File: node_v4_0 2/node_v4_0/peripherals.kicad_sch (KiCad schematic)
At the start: 26 parts, among them J3 Conn_Coaxial, U10 MCP7940N-xP, U11 1042240820, U12 CAT24M01W, U6 RFM69HCW, U9 SIM7080G

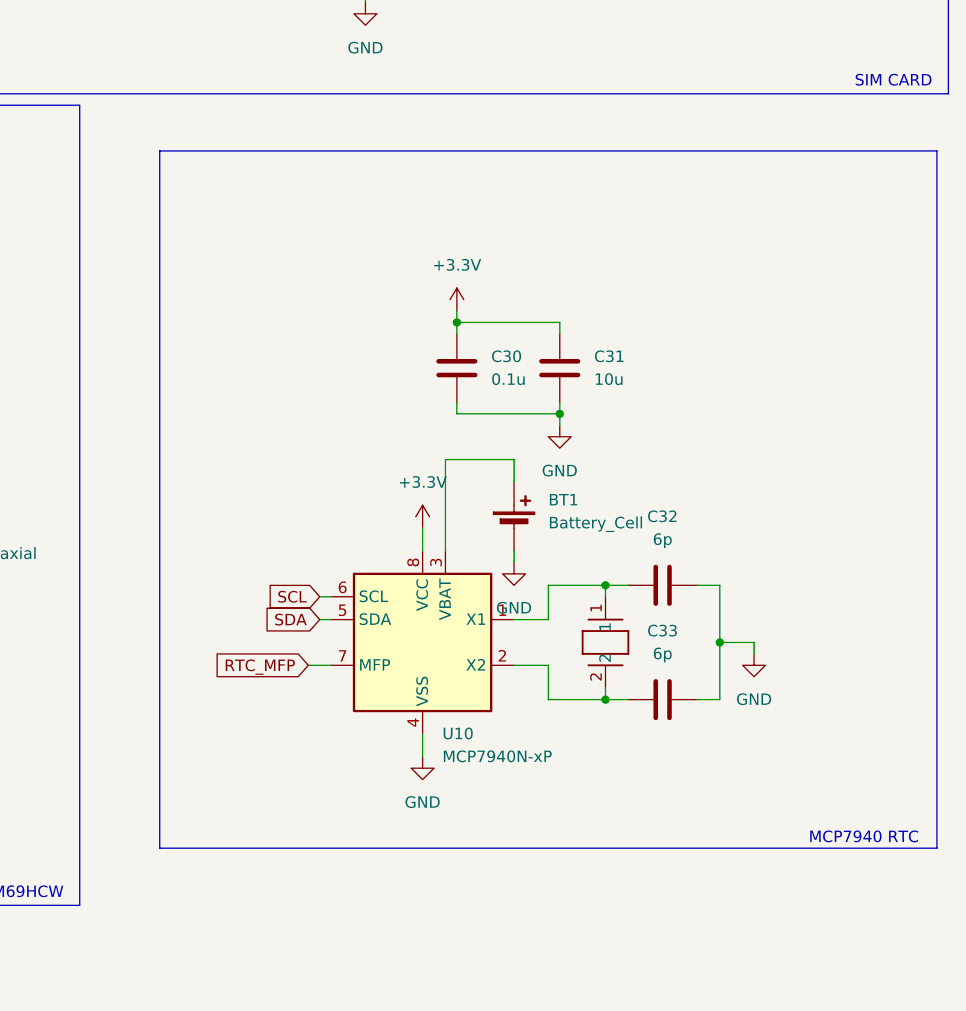
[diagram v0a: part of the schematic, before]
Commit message: finished laying out the board
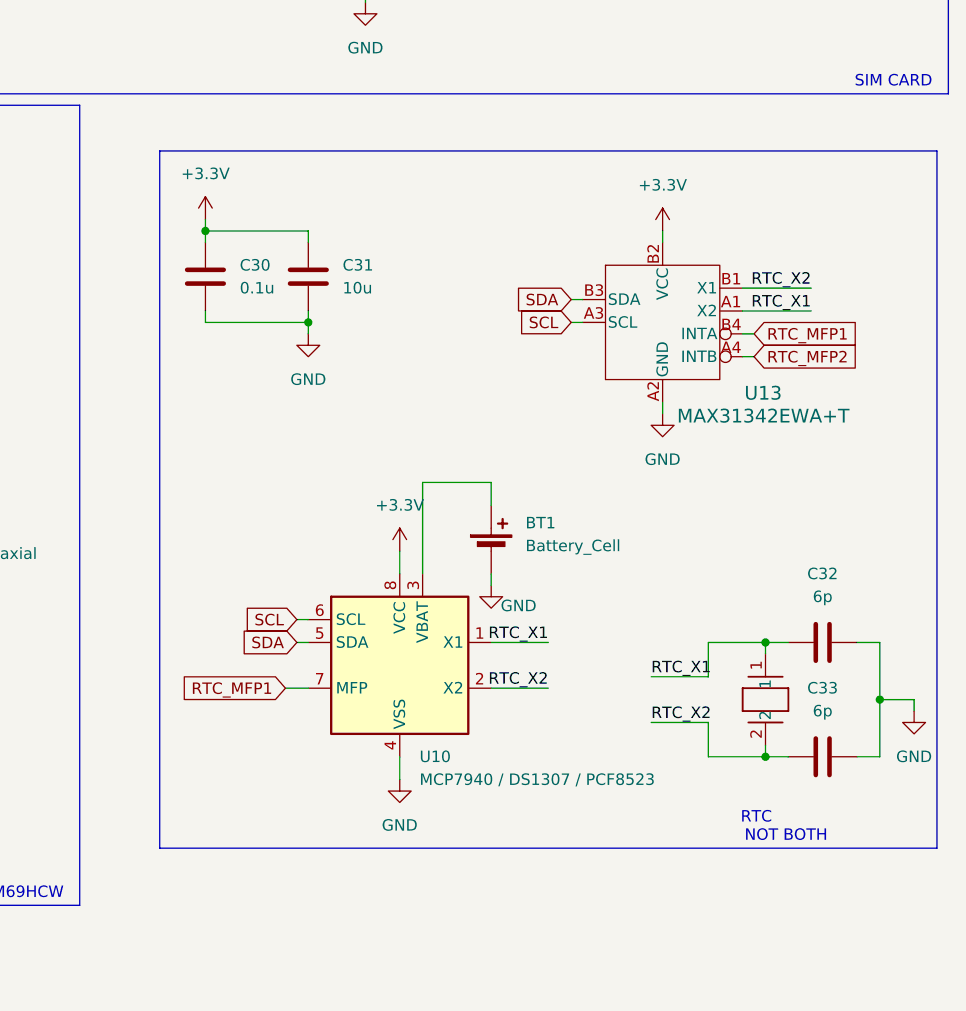
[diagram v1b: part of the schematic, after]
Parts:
- added U13: MAX31342EWA+T, WiSDOM:21-100291_W80D&plus_1_MXM, symbol WiSDOM:MAX31342EWA+T
- R14, R15: footprint Resistor_SMD:R_0805_2012Metric_Pad1.20x1.40mm_HandSolder -> Resistor_SMD:R_0402_1005Metric_Pad0.72x0.64mm_HandSolder
- U10: value MCP7940N-xP -> MCP7940 / DS1307 / PCF8523
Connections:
- net +3.3V: now also U13.B2 (VCC)
- net GND: now also U13.A2 (GND)
- net SCL: now also U13.A3 (SCL)
- net SDA: now also U13.B3 (SDA)
- net RTC_X2: now reaches C33.1, U10.2 (X2), XTAL1.2
- net RTC_X2: now also U13.B1 (X1)
- net RTC_X1: now reaches C32.1, U10.1 (X1), XTAL1.1
- net RTC_X1: now also U13.A1 (X2)
- net RTC_MFP renamed RTC_MFP1
- net RTC_MFP1: now also U13.B4 (INTA)
- new net RTC_MFP2: U13.A4 (INTB)
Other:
- note added: "NOT BOTH"
- note added: "RTC"
- note removed: "MCP7940 RTC"
- moved on the sheet: BT1, C30, C31, C32, C33, U10

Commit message: most routing done
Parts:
- removed BT1: Battery_Cell, WiSDOM:BAT_BAT-HLD-001-THM, symbol Device:Battery_Cell
- added C44: 0.1u, Capacitor_SMD:C_0402_1005Metric_Pad0.74x0.62mm_HandSolder, symbol Device:C
- added C45: 10u, Capacitor_SMD:C_0805_2012Metric_Pad1.18x1.45mm_HandSolder, symbol Device:C
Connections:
- net +3.3V: now also C44.1, C45.1; no longer U13.B2 (VCC)
- net GND: now also C44.2, C45.2
- net RTC_BAT: now reaches U10.3 (VBAT)
- new net +VRTC: U13.B2 (VCC)
